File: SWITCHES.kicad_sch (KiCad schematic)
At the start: 28 parts, among them U2 LP5012RUKR

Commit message: Footprint inspections and cleanups.
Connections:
- net GNDD: now also S2.MP1, S2.MP2, S2.MP3, S2.MP4
- net LED SCL renamed LEDSCL

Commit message: Electrical Rules Check fixes in progress.
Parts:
- added C9: 0.1uF, Mustang_Library:C_0805_2012Metric_Pad1.18x1.45mm_HandSolder, symbol Mustang_Library:CAP_CERAMIC0805-NOOUTLINE
- added R13, R14: 0R, symbol Mustang_Library:R_h
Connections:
- net +3V3: now also C9.1
- net SW_BTPAIR: now reaches C145.2, D8.2, R79.1
- net SW_PWR: now reaches C144.2, D7.2, R77.1
- net GND: now reaches S3.MP1
- net GND: now also C141.1, C142.1, C143.1, C144.1, C145.1, D1.1, D2.1, D7.1, D8.1, R76.2, S1.1 (NO_1), S1.2 (NO_2), S1.7 (NC_3), S2.2 (NO), S2.MP1, S2.MP2, S2.MP3, S2.MP4, S3.2 (NO), S3.MP2, S3.MP3, S3.MP4, U2.21 (Therm/GND), C9.2, R13.1, R14.1
- net BT_PAIR: no longer names the net of R79.2, R80.1, S1.5 (NO_3)
- removed net GNDD: C141.1, C142.1, C143.1, C144.1, C145.1, D1.1, D2.1, D7.1, D8.1, R76.2, S1.1 (NO_1), S1.2 (NO_2), S1.7 (NC_3), S2.2 (NO), S2.MP1, S2.MP2, S2.MP3, S2.MP4, S3.2 (NO), U2.14 (ADDR0), U2.15 (ADDR1), U2.21 (Therm/GND)
- net LEDSCL renamed LED_SCL
- net LEDSDA renamed LED_SDA
- net MCU_PWR: no longer names the net of R77.2, R78.1, S1.3 (NC_1)
- net MCU_Record renamed SW_RECORD
- net TOMCUGPIO renamed SW_PLAY
- new net: R14.2, U2.15 (ADDR1)
- new net: R13.2, U2.14 (ADDR0)
- no-connect marks 10 -> 2
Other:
- note added: "Play"
- moved on the sheet: C141, C142, D1, D2, D8, R45, R71, R72, R73, R74, R75, R76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

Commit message: wip
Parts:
- added C22, C23, C24, C25: 0.1uF, Mustang_Library:C_0805_2012Metric_Pad1.18x1.45mm_HandSolder, symbol Mustang_Library:CAP_CERAMIC0805-NOOUTLINE
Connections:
- net +3V3: now also C22.1, C23.1, C24.1, C25.1
- net GND: now also C22.2, C23.2, C24.2, C25.2

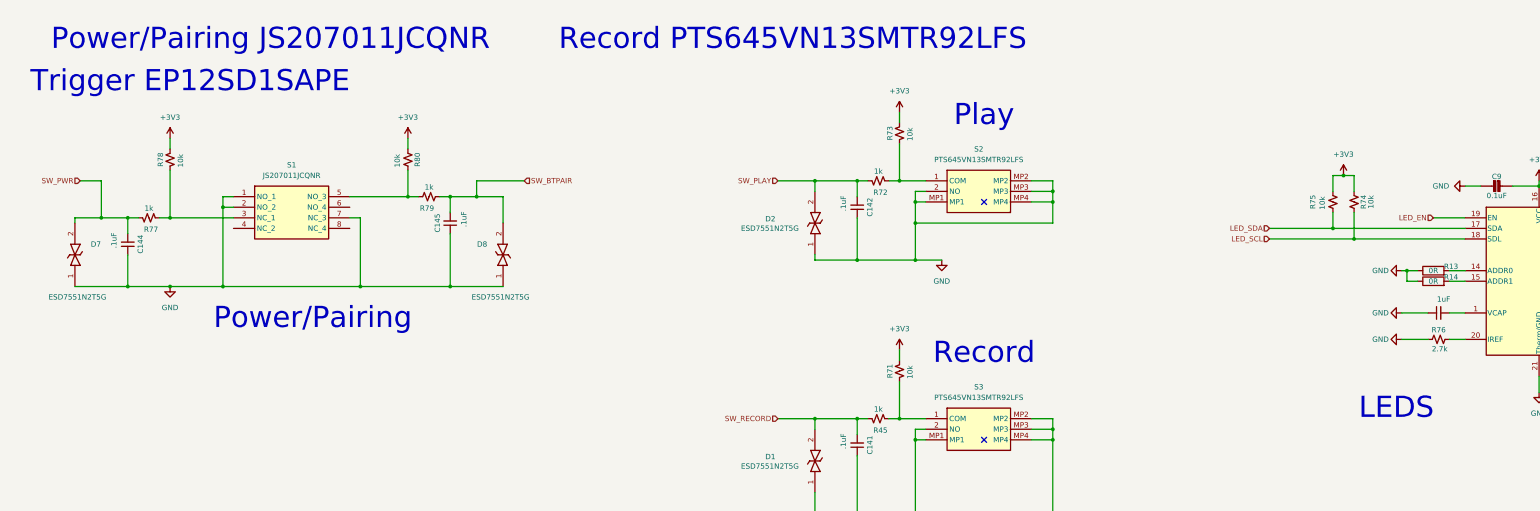
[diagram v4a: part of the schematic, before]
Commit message: Use all YAGEO 0603 resistors.
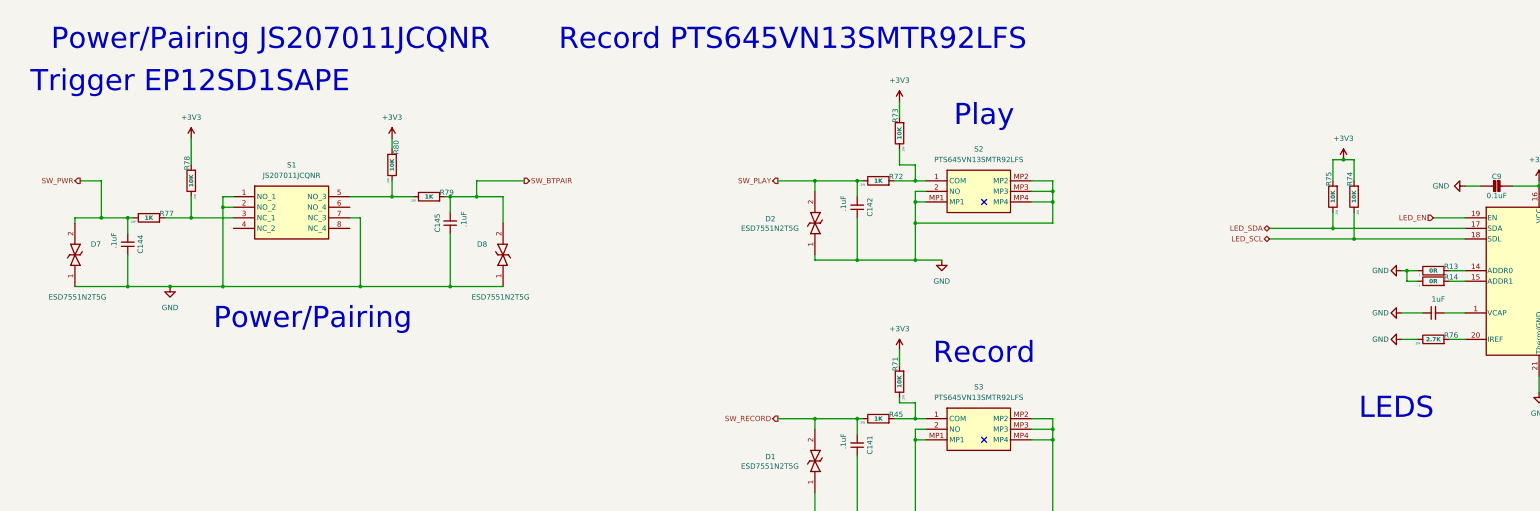
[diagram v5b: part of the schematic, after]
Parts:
- C141, C142, C143, C144, C145: footprint Mustang_Library:C_0402_1005Metric -> Mustang_Library:C_0805_2012Metric_Pad1.18x1.45mm_HandSolder
- R13, R14: footprint (none) -> Mustang_Library:R_0603_1608Metric; symbol Mustang_Library:R_h -> Mustang_Library:R_0603_0R; MPN (none) -> AC0603JR-070RL; Manufacturer (none) -> Yageo; Power (none) -> J
- R45, R72, R77, R79: value 1k -> 1K; footprint Mustang_Library:R_0402_1005Metric -> Mustang_Library:R_0603_1608Metric; symbol Mustang_Library:R_Small_US -> Mustang_Library:R_0603_1K; MPN (none) -> AC0603FR-7W1KL; Manufacturer (none) -> Yageo; Manufacturer_Part_Number RC0402FR-7D1KL -> (none); Power (none) -> .2W
- R71, R73, R74, R75, R78, R80: value 10k -> 10K; footprint Mustang_Library:R_0402_1005Metric -> Mustang_Library:R_0603_1608Metric; symbol Mustang_Library:R_Small_US -> Mustang_Library:R_0603_10K; MPN (none) -> AC0603FR-7W10KL; Manufacturer (none) -> Yageo; Manufacturer_Part_Number CRCW040210K0FKEDC -> (none); Power (none) -> .2W
- R76: value 2.7k -> 2.7K; footprint Mustang_Library:R_0402_1005Metric -> Mustang_Library:R_0603_1608Metric; symbol Mustang_Library:R_Small_US -> Mustang_Library:R_0603_2.7K; MPN (none) -> AC0603FR-072K7L; Manufacturer (none) -> Yageo; Manufacturer_Part_Number CRCW04022K70JNTD -> (none); Power (none) -> .1W
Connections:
- net GND: now also R76.1; no longer R76.2
- net SW_BTPAIR: now also R79.2; no longer R79.1
- net at R80.1, S1.5 (NO_3): now also R79.1; no longer R79.2
- net at U2.20 (IREF): now also R76.2; no longer R76.1
